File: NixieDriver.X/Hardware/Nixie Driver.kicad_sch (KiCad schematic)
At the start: 18 parts, among them J1 HDR-2X3, J2 HDR-2X3, Q0 MMBTA42LT1G, Q1 MMBTA42LT1G, Q10 MMBTA42LT1G, Q2 MMBTA42LT1G, Q3 MMBTA42LT1G, Q4 MMBTA42LT1G, Q5 MMBTA42LT1G, Q6 MMBTA42LT1G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

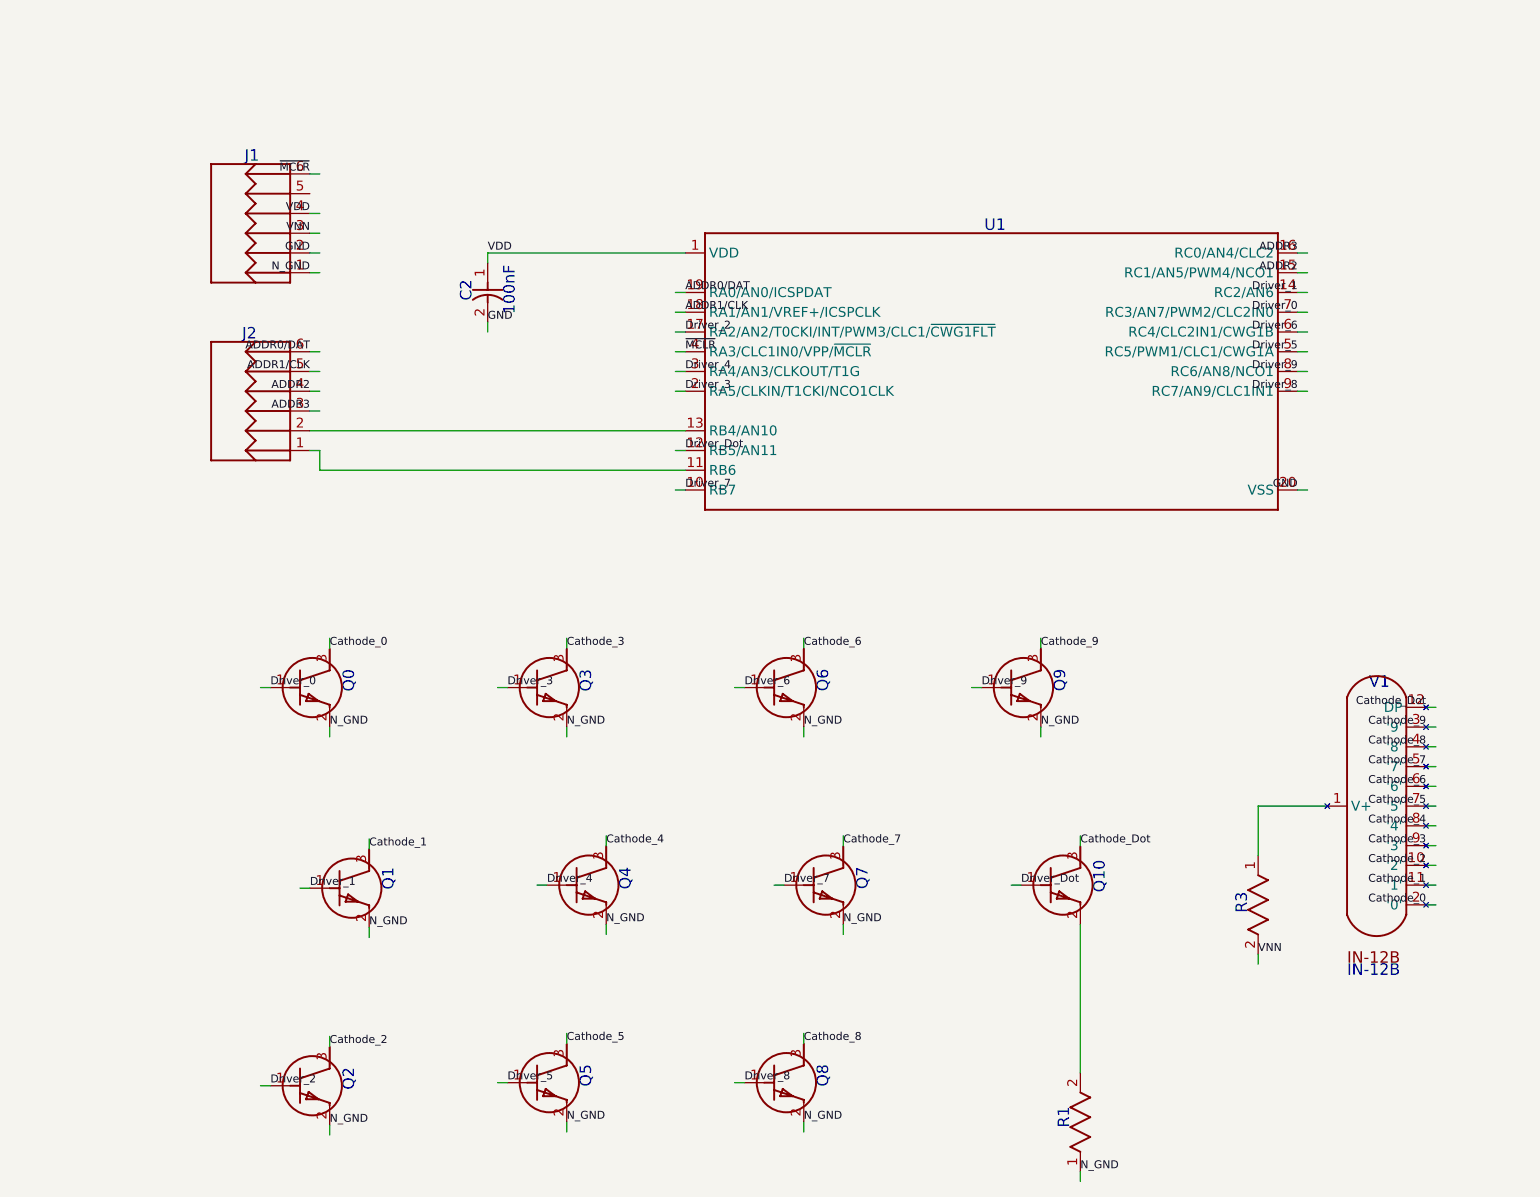
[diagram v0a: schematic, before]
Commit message: Migration from DipTrace. Updated symbols and footprints.
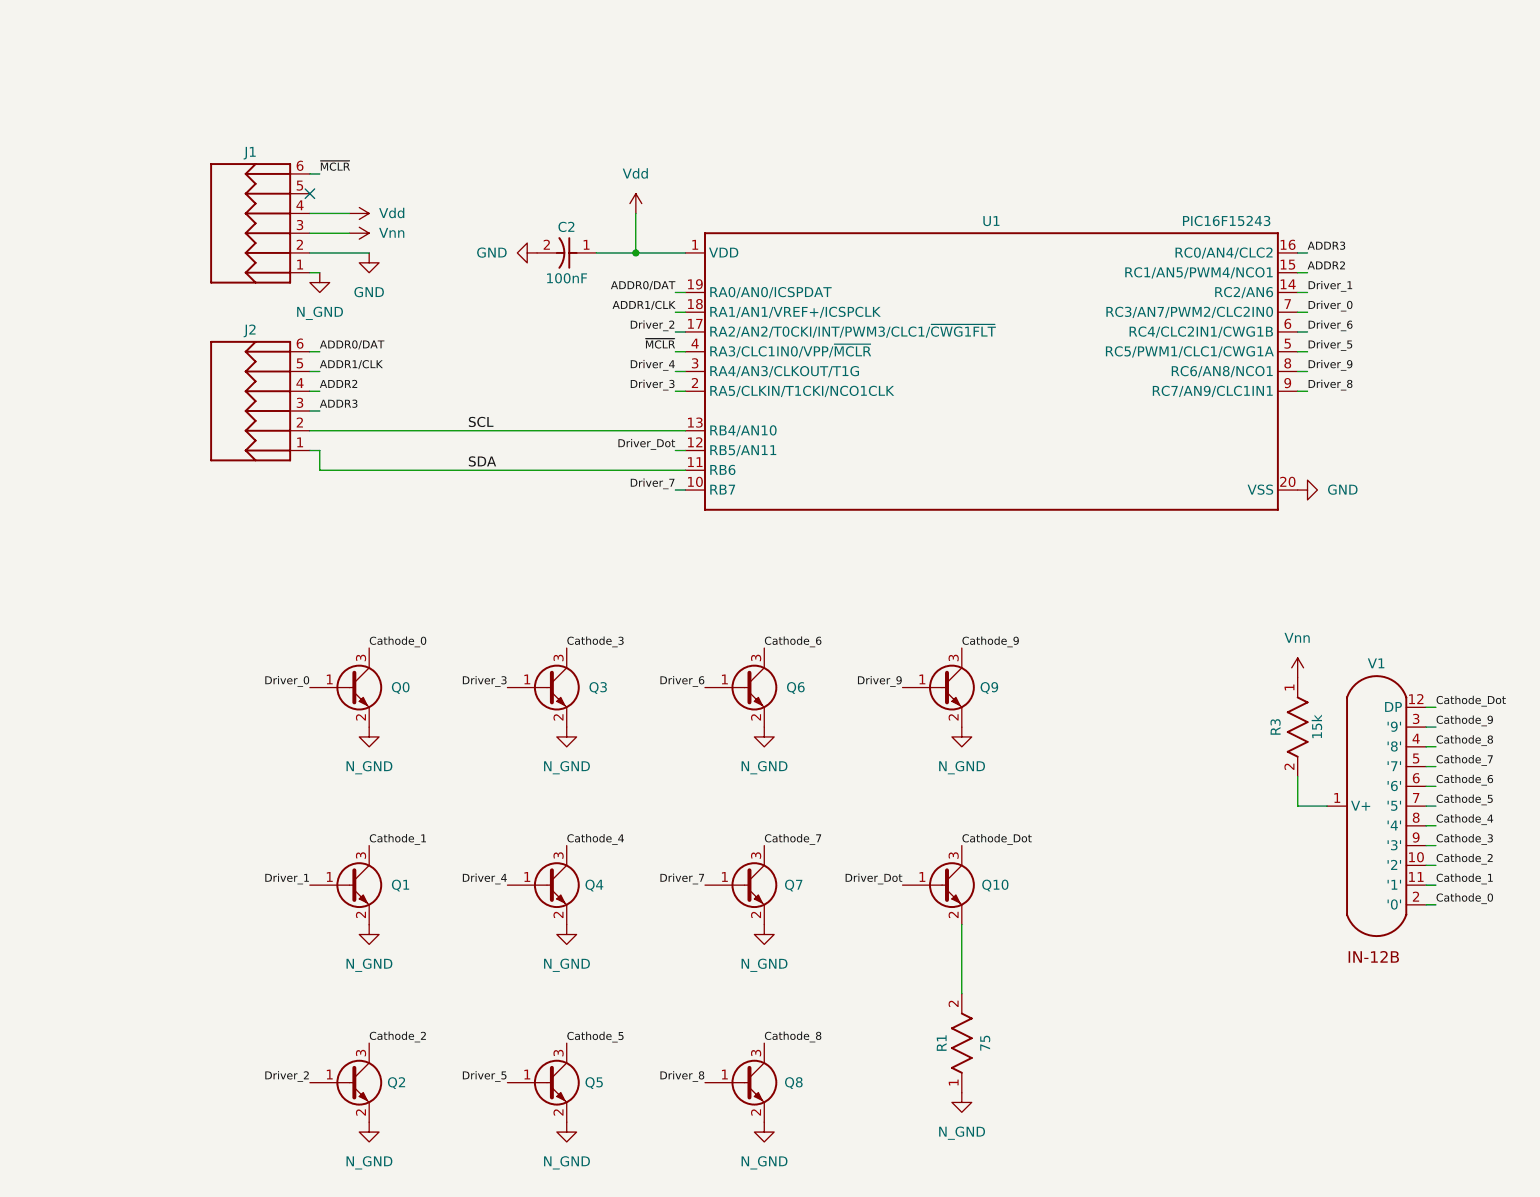
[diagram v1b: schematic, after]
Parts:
- C2: footprint Nixie Driver:CAP_0603 -> Capacitor_SMD:C_0603_1608Metric
- J1, J2: footprint Nixie Driver:HDR-2X3 -> Connector_PinHeader_2.54mm:PinHeader_2x03_P2.54mm_Vertical
- Q0, Q1, Q10, Q2, Q3, Q4, Q5, Q6, Q7, Q8, Q9: footprint Nixie Driver:SOT23-3P95_240X110L43X44N -> Package_TO_SOT_SMD:SOT-23; symbol Nixie Driver-eagle-import:MMBTA42LT1G -> Transistor_BJT:MMBTA42
- R1, R3: footprint Nixie Driver:RES_1206 -> Resistor_SMD:R_1206_3216Metric
- U1: value 100nF -> PIC16F15243; footprint Nixie Driver:SOP20P65_720X770X160L50X30N -> Package_SO:SSOP-20_5.3x7.2mm_P0.65mm
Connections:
- net Cathode_8: now also Q8.3 (C)
- net Driver_0: now also Q0.1 (B)
- net Driver_3: now also Q3.1 (B)
- net Driver_4: now also Q4.1 (B)
- net Driver_6: now also Q6.1 (B)
- net Driver_7: now also Q7.1 (B)
- net Driver_9: now also Q9.1 (B)
- net Driver_Dot: now also Q10.1 (B)
- net N_GND: now also Q0.2 (E), Q3.2 (E), Q4.2 (E), Q6.2 (E), Q7.2 (E), Q9.2 (E)
- net SDA: now reaches J2.1 (P1), U1.11 (RB6)
- net SCL: now reaches J2.2 (P2), U1.13 (RB4/AN10)
- net at V1.1 (V+): now also R3.2; no longer R3.1
- net at Q10.2 (E): now also R1.2
- net VDD renamed Vdd
- net VNN renamed Vnn
- net Vnn: now also R3.1; no longer R3.2
- no-connect marks 0 -> 1
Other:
- note removed: "100nF"
- note removed: "C2"
- note removed: "IN-12B"
- note removed: "J1"
- note removed: "J2"
- note removed: "Q0"
- note removed: "Q1"
- note removed: "Q10"
- note removed: "Q2"
- note removed: "Q3"
- note removed: "Q4"
- note removed: "Q5"
- note removed: "Q6"
- note removed: "Q7"
- note removed: "Q8"
- note removed: "Q9"
- note removed: "R1"
- note removed: "R3"
- note removed: "U1"
- note removed: "V1"

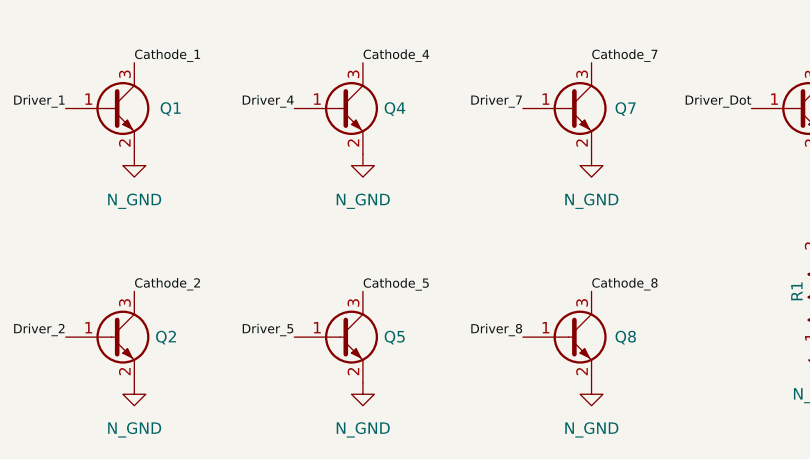
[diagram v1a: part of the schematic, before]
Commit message: Fixed header position
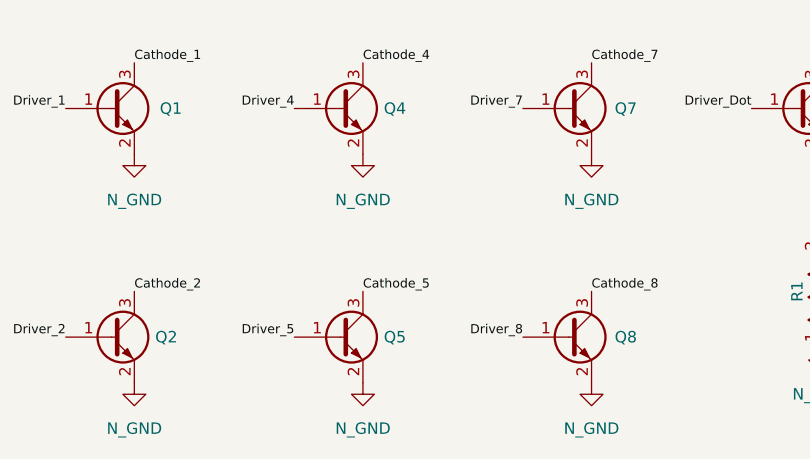
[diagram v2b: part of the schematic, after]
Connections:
- net Cathode_5: now also Q5.3 (C)
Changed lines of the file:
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@@
 	)
 	(label "Cathode_5"
-		(at 114.3 152.413 0)
+		(at 114.3 152.4 0)
 		(fields_autoplaced yes)
 		(effects

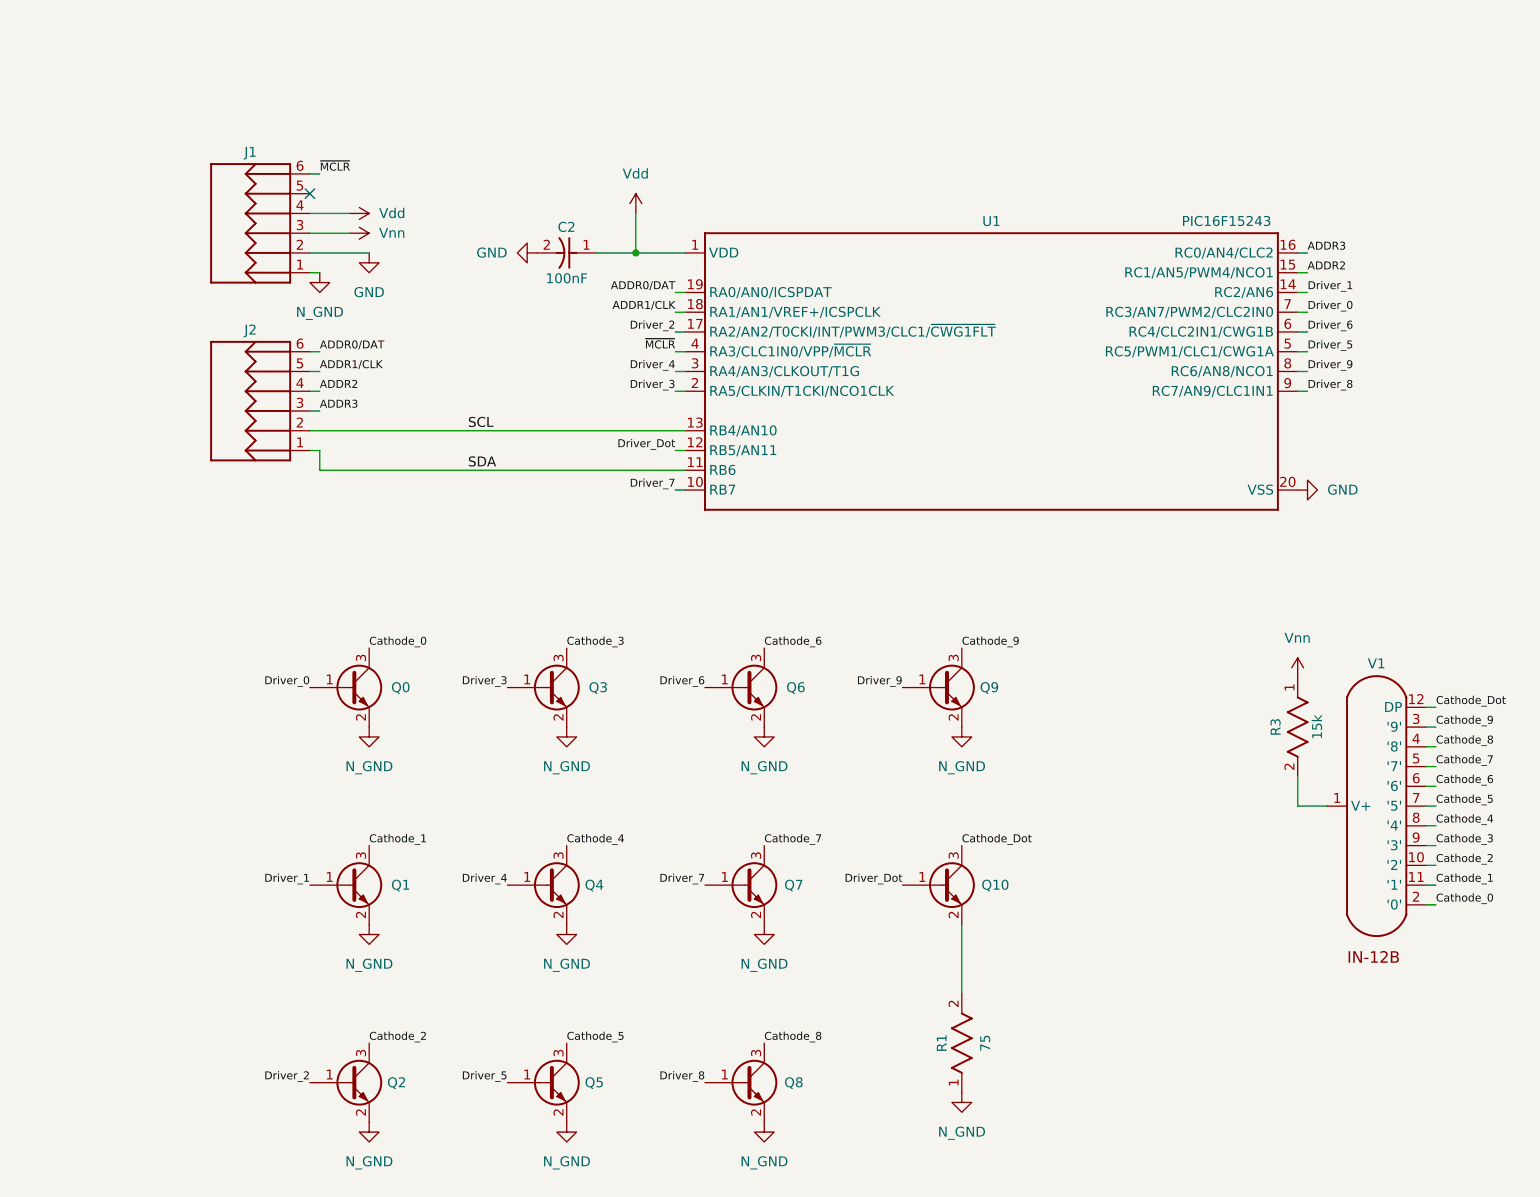
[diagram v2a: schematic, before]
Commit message: Minimal fix for missing current limiting resistor
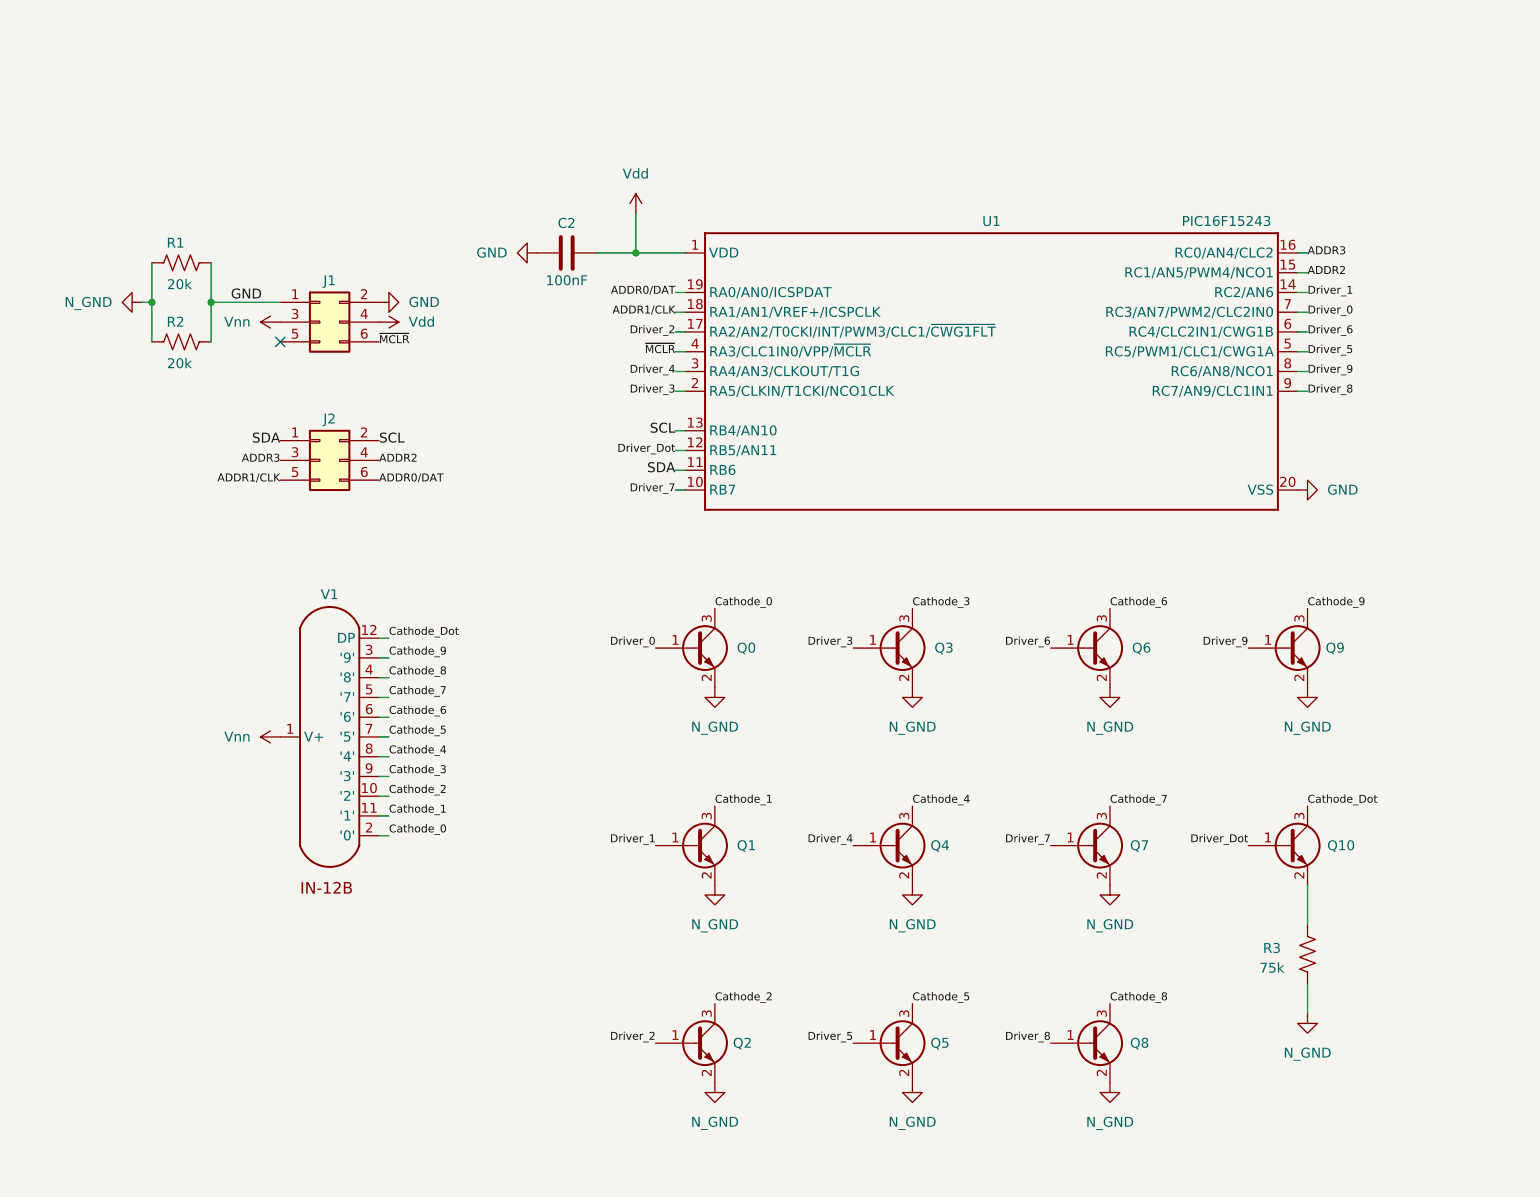
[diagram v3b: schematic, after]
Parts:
- removed J1, J2: HDR-2X3, Connector_PinHeader_2.54mm:PinHeader_2x03_P2.54mm_Vertical, symbol Nixie Driver-eagle-import:HDR-2X3
- added J1, J2: Conn_02x03_Odd_Even, Connector_PinHeader_2.54mm:PinHeader_2x03_P2.54mm_Vertical, symbol Connector_Generic:Conn_02x03_Odd_Even
- added R2: 20k, Resistor_SMD:R_1206_3216Metric, symbol Device:R_US
- C2: symbol Nixie Driver-eagle-import:CAP_0603 -> Device:C
- R1: renamed from R3; value 15k -> 20k; symbol Nixie Driver-eagle-import:RES_1206 -> Device:R_US
- R3: renamed from R1; value 75 -> 75k; symbol Nixie Driver-eagle-import:RES_1206 -> Device:R_US
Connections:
- net ADDR0/DAT: now also J2.6 (Pin_6)
- net ADDR1/CLK: now also J2.5 (Pin_5)
- net ADDR2: now also J2.4 (Pin_4)
- net ADDR3: now also J2.3 (Pin_3)
- net GND: now also R1.2, J1.1 (Pin_1), J1.2 (Pin_2), R2.2
- net N_GND: now also R1.1, R2.1
- net SCL: now also J2.2 (Pin_2)
- net SDA: now also J2.1 (Pin_1)
- net Vdd: now also J1.4 (Pin_4)
- net Vnn: now also V1.1 (V+), J1.3 (Pin_3); no longer R1.1
- net ~{MCLR}: now also J1.6 (Pin_6)
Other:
- moved on the sheet: Q0, Q1, Q10, Q2, Q3, Q4, Q5, Q6, Q7, Q8, Q9, V1

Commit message: Reduced resistor size to 0805
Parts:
- R1, R2, R3: footprint Resistor_SMD:R_1206_3216Metric -> Resistor_SMD:R_0805_2012Metric
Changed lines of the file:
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@@
 			)
 		)
-		(property "Footprint" "Resistor_SMD:R_1206_3216Metric"
+		(property "Footprint" "Resistor_SMD:R_0805_2012Metric"
 			(at 65.024 51.054 90)
 			(effects
@@
 			)
 		)
-		(property "Footprint" "Resistor_SMD:R_1206_3216Metric"
+		(property "Footprint" "Resistor_SMD:R_0805_2012Metric"
 			(at 65.024 61.214 90)
 			(effects
@@
 			)
 		)
-		(property "Footprint" "Resistor_SMD:R_1206_3216Metric"
+		(property "Footprint" "Resistor_SMD:R_0805_2012Metric"
 			(at 208.534 140.716 90)
 			(effects

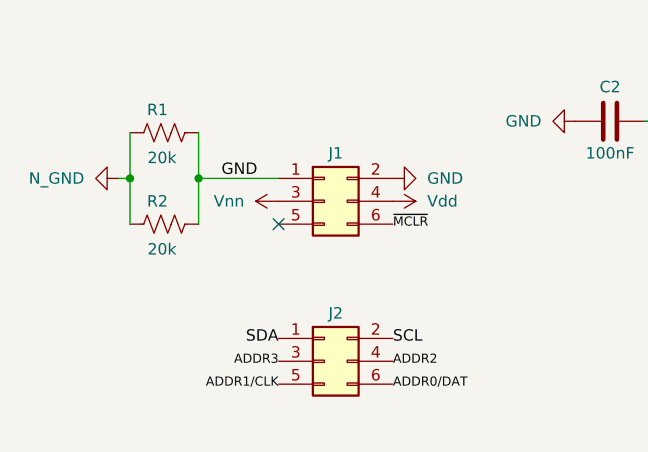
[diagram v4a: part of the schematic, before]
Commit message: Separated the grounds so the test harness will still work.
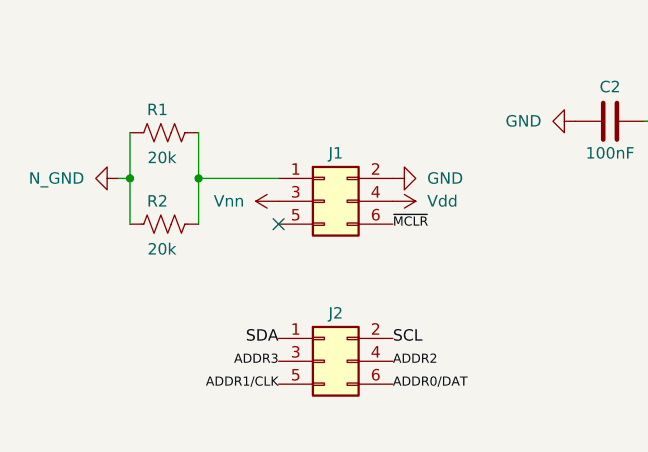
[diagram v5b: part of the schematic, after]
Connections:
- net GND: no longer J1.1 (Pin_1), R1.2, R2.2
- new net: J1.1 (Pin_1), R1.2, R2.2
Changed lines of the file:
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@@
-		)
-	)
-	(label "GND"
-		(at 71.12 57.15 0)
-		(fields_autoplaced yes)
-		(effects
-			(font
-				(size 1.27 1.27)
-			)
-			(justify left bottom)
 		)
 	)
